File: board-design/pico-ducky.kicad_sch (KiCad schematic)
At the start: 6 parts, among them J1 Conn_01x20_Female, J2 Conn_01x20_Female, SW3 SK-14D01-G_6, U1 Pico

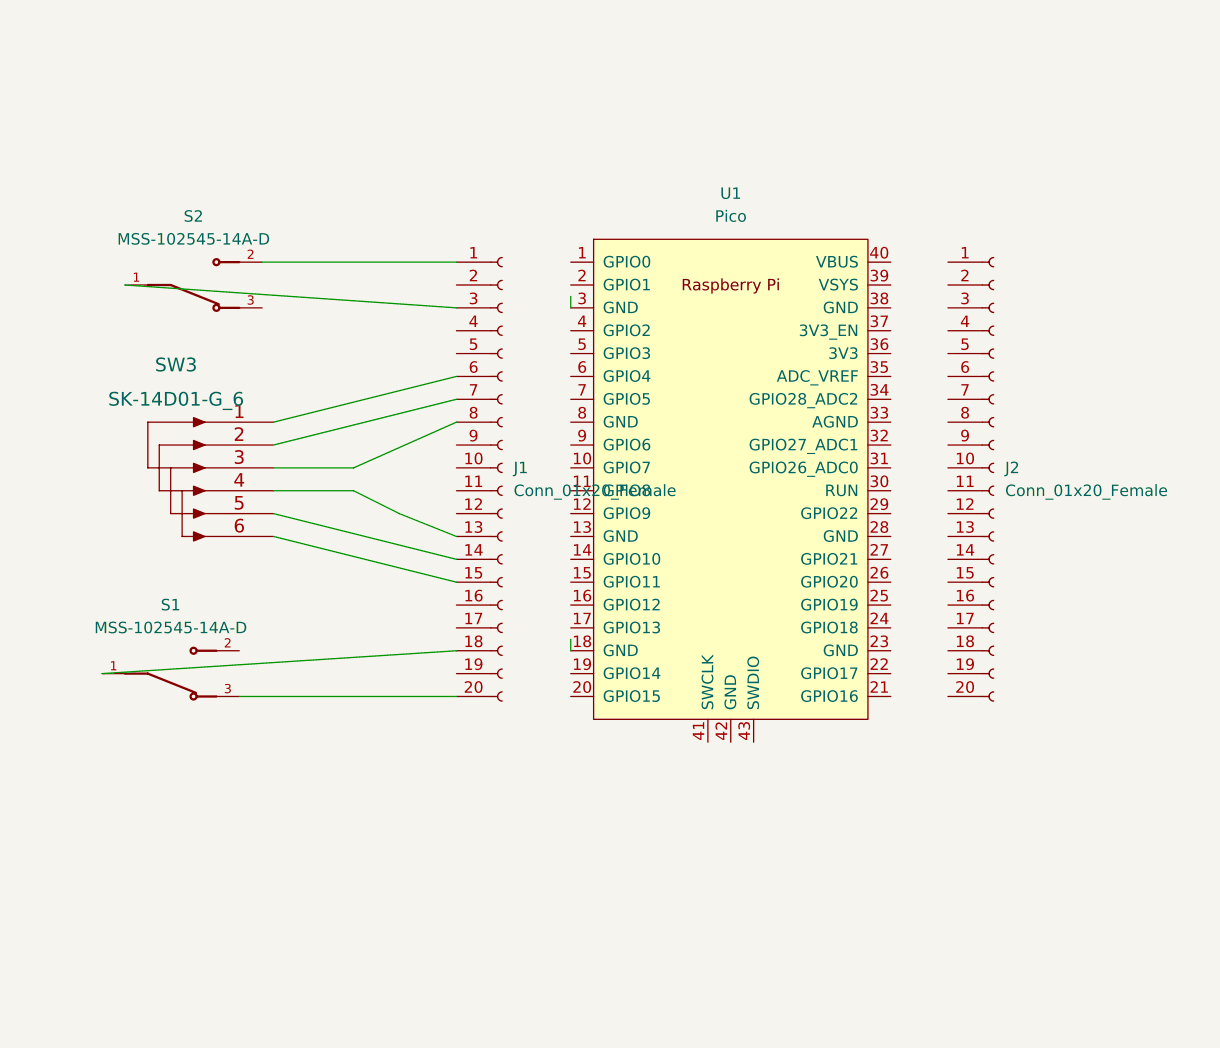
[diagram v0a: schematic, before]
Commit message: Added microSD reader and changed switches
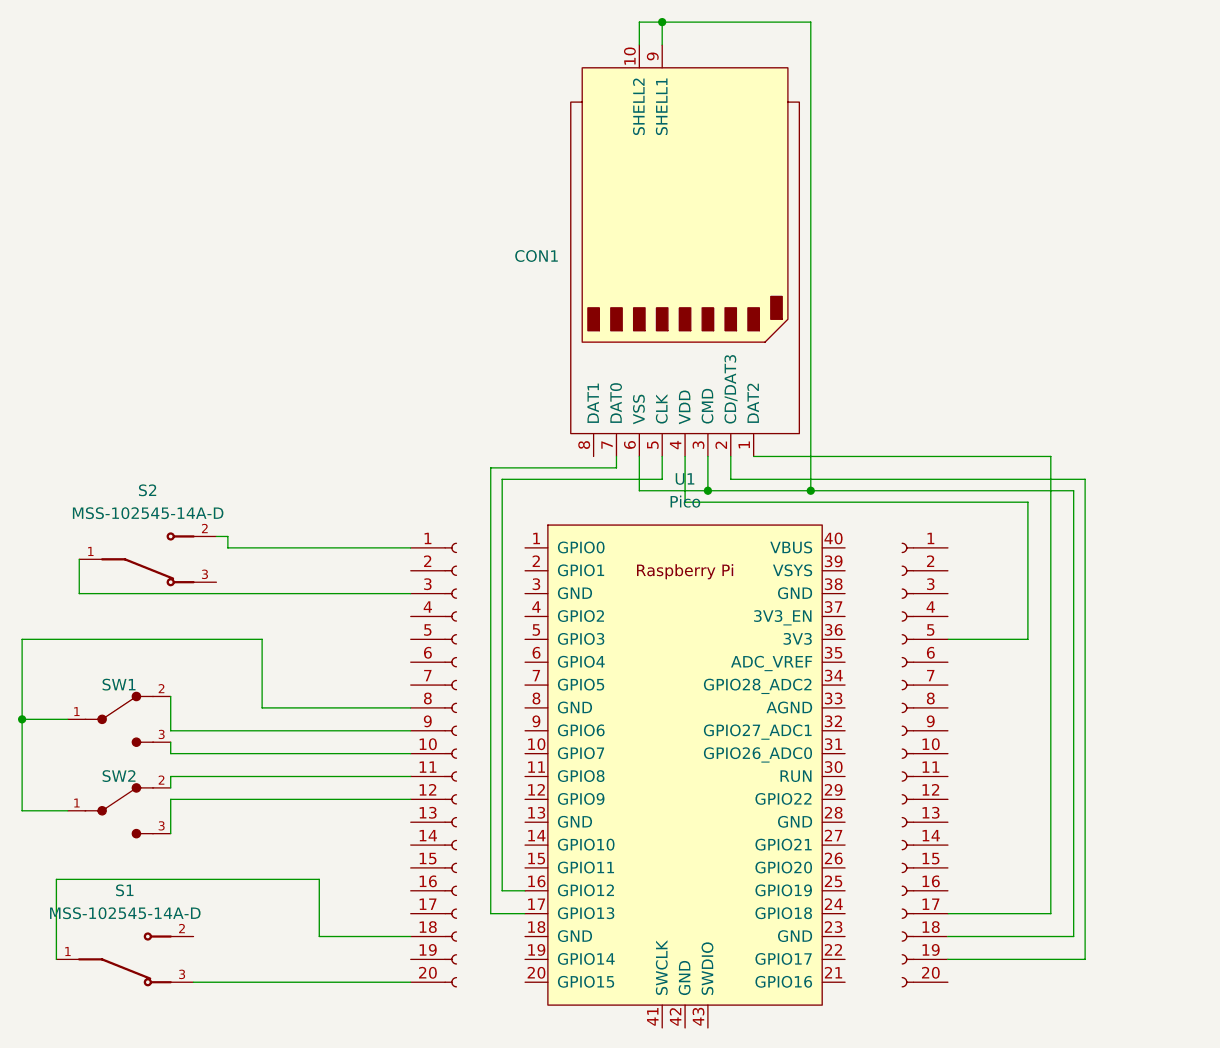
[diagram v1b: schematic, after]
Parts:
- removed SW3: SK-14D01-G_6, SK-14D01-G6:SK-14D01-G 6, symbol 2022-01-11_23-37-23:SK-14D01-G_6
- added CON1: ~, PCM_4ms_Connector_Card:CardSlot_MicroSD_YamaichiPJS008U-3000, symbol PCM_4ms_Connector:microSDCon_Vert_TH_PJS008U-3000
- added SW1, SW2: ~, PCM_CB_Devices:Slide_Switch_SPDT_P3mm_10x5x10mm, symbol PCM_CB_Devices:Slide_Switch_SPDT_P3mm_10x5x10mm
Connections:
- net at U1.16 (GPIO12): now also CON1.5 (CLK)
- net at U1.17 (GPIO13): now also CON1.7 (DAT0)
- net at J1.10 (Pin_10): now also SW1.3
- net at J1.11 (Pin_11): now also SW2.2
- net at J1.12 (Pin_12): now also SW2.3
- net at J1.8 (Pin_8): now also SW1.1, SW2.1
- net at J1.9 (Pin_9): now also SW1.2
- net at J2.17 (Pin_17): now also CON1.1 (DAT2)
- net at J2.18 (Pin_18): now also CON1.10 (SHELL2), CON1.3 (CMD), CON1.6 (VSS), CON1.9 (SHELL1)
- net at J2.19 (Pin_19): now also CON1.2 (CD/DAT3)
- net at J2.5 (Pin_5): now also CON1.4 (VDD)
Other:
- moved on the sheet: S1, S2, U1
